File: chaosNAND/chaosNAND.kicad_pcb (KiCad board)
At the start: 2 copper layers, 49.3 x 37.5 mm, 23 parts, among them CON1 BARREL_JACK, J1 JACK_MONO, SW1 SPST, SW2 SWITCH_INV, SW3 SWITCH_INV, U1 4093

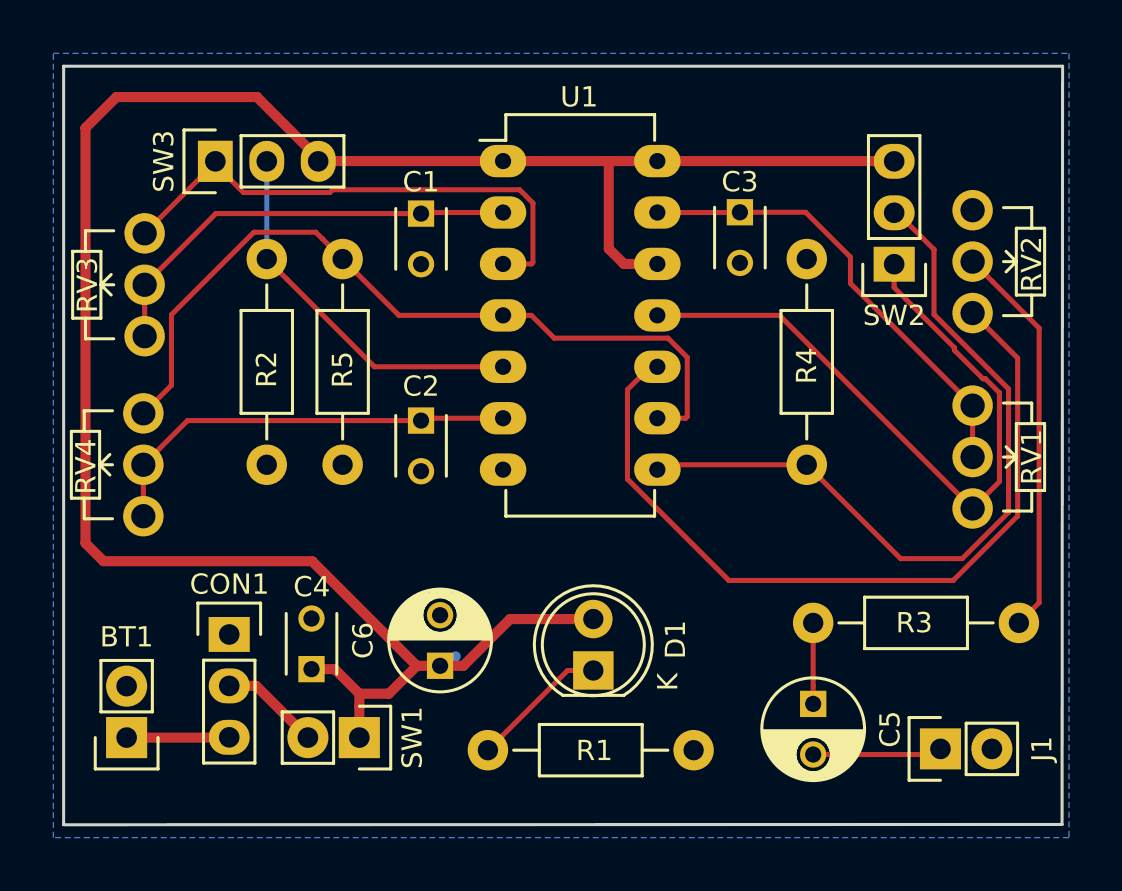
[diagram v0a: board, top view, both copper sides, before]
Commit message: added c-base markings to the PCB
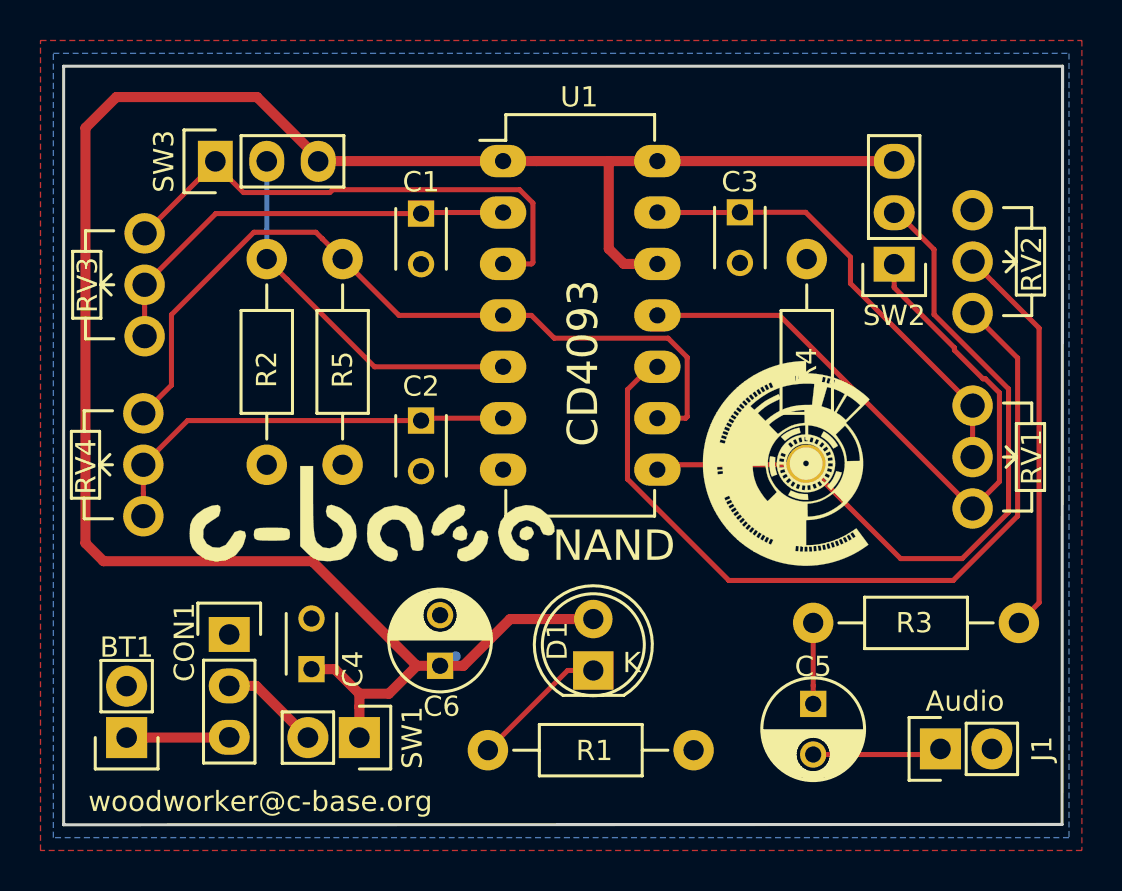
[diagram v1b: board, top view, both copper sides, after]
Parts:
- added G***: LOGO, kicad-cbase:c-base-logo-ceva, F.Cu at (185.9, 104.7)
- added G***: LOGO, kicad-cbase:c-base, F.Cu at (206.4, 102.2)
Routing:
- added copper zone on F.Cu, net GND
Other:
- board text added: "Audio"
- board text added: "CD4093"
- board text added: "NAND"
- board text added: "woodworker@c-base.org"

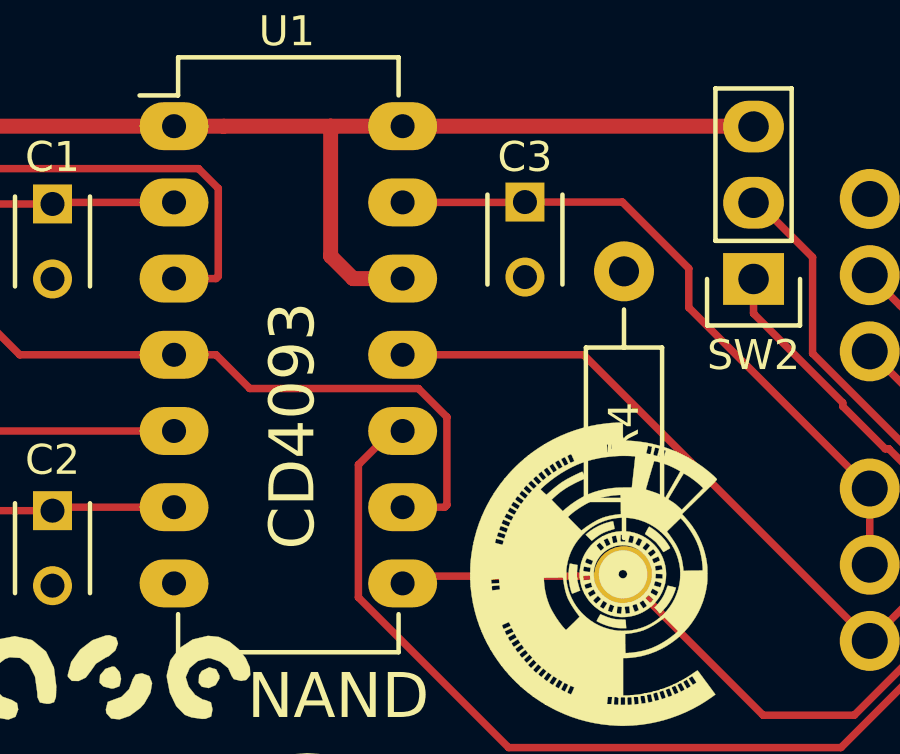
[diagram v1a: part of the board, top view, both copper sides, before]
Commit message: more silkscreen
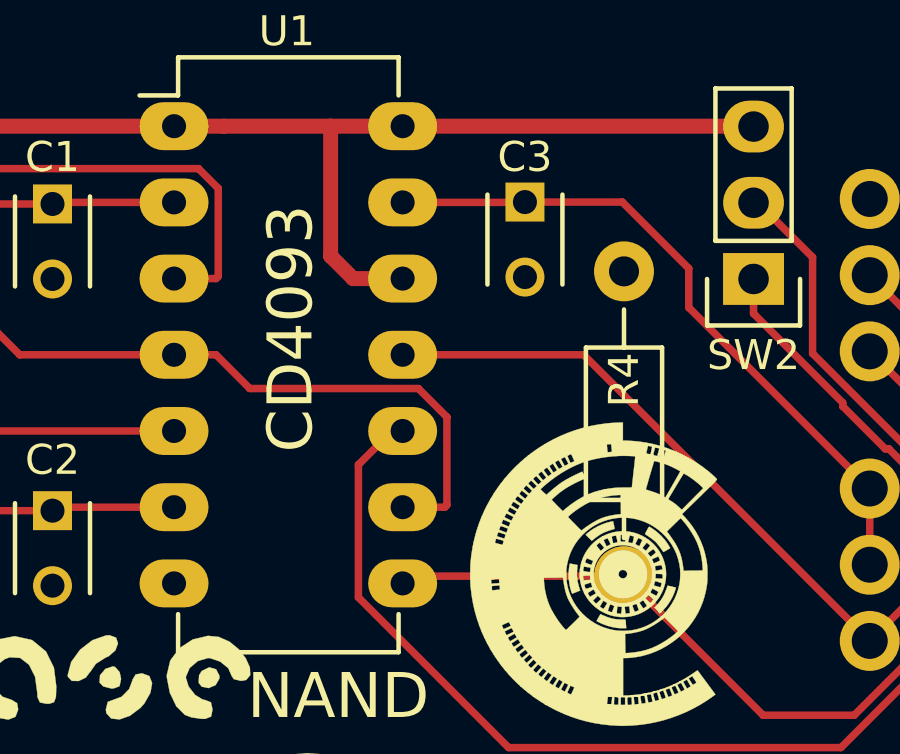
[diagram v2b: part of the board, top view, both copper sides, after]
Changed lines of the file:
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@@
     (descr "Resistor, Axial,  RM 10mm, 1/3W")
     (tags "Resistor Axial RM 10mm 1/3W")
-    (fp_text reference R4 (at 4.8895 0 90) (layer F.SilkS)
+    (fp_text reference R4 (at 6.5405 0 90) (layer F.SilkS)
       (effects (font (size 1 1) (thickness 0.15)))
     )
@@
     (effects (font (size 1 1) (thickness 0.2)))
   )
-  (gr_text CD4093 (at 196.342 97.2185 90) (layer F.SilkS)
+  (gr_text CD4093 (at 196.2785 93.98 90) (layer F.SilkS)
     (effects (font (size 1.5 1.5) (thickness 0.3)))
   )
